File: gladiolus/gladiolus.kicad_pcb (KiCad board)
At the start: 4 copper layers, 70.7 x 53.3 mm, 138 parts, among them J1 NEIGHBOR1, J2 NEIGHBOR2, J3 Conn_01x02_Female, J7 BONUS_ROW, Q1 Q_NPN_BEC, U1 THS4520RGT, U2 AD8330ARQZ, U3 AD9283, U4 AD9704, U5 LMH6643, U6 74LVC1G3157, U7 74LVC1G3157

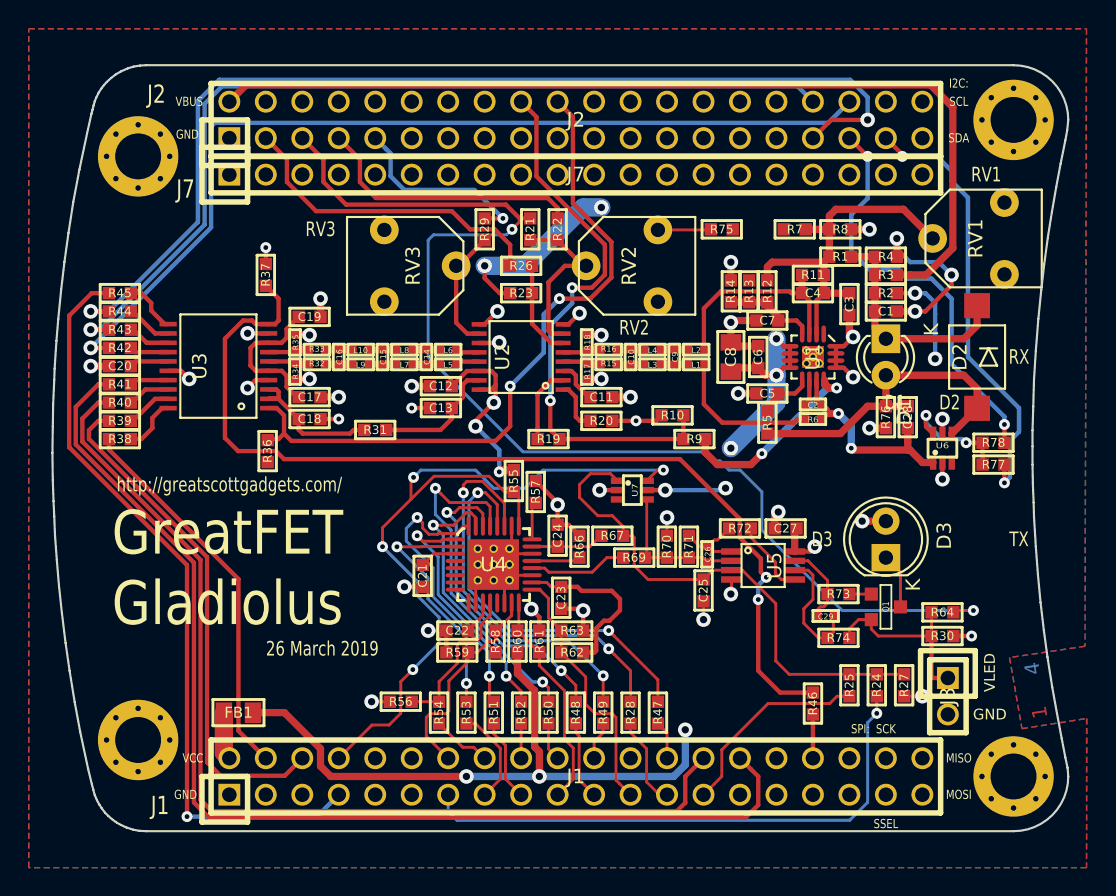
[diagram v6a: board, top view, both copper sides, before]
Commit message: Rerouted ADC trace to improve ground plane connectivity
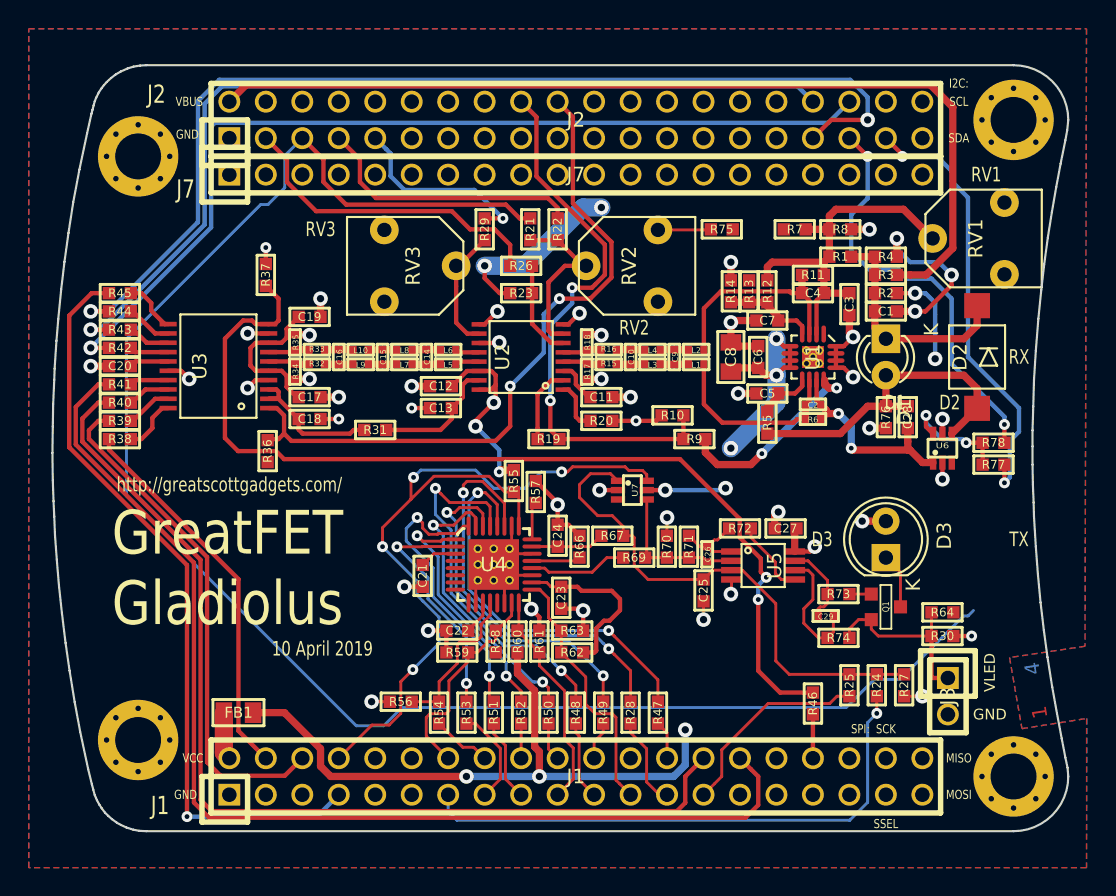
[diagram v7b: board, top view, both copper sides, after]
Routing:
- net /ADC0_0: track 83.9 -> 118.3 mm, vias 2 -> 0
- net /P5_0: track 56.6 -> 54.7 mm
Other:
- board text added: "10 April 2019"
- board text removed: "26 March 2019"
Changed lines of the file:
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@@
     (thickness 1.6)
     (drawings 133)
-    (tracks 1068)
+    (tracks 1066)
     (zones 0)
     (modules 138)
@@
     (pad_drill 0.762)
     (pad_to_mask_clearance 0.127)
-    (solder_mask_min_width 0.25)
     (pad_to_paste_clearance_ratio -0.05)
     (aux_axis_origin 0 0)
@@
   (gr_line (start 177.9016 92.3544) (end 177.8508 94.0054) (angle 90) (layer Edge.Cuts) (width 0.15))
   (gr_line (start 177.9524 90.5002) (end 177.9016 92.3544) (angle 90) (layer Edge.Cuts) (width 0.15))
-  (gr_text "26 March 2019" (at 128.397 109.22) (layer F.SilkS)
+  (gr_text "10 April 2019" (at 128.397 109.22) (layer F.SilkS)
     (effects (font (size 1.016 0.762) (thickness 0.1524)))
   )
@@
   (segment (start 134.569198 98.806) (end 132.588 100.787198) (width 0.2032) (layer F.Cu) (net 26))
   (segment (start 136.169411 97.205787) (end 134.569198 98.806) (width 0.2032) (layer F.Cu) (net 26))
-  (via (at 152.146 96.774) (size 0.762) (drill 0.3302) (layers F.Cu B.Cu) (net 26))
-  (segment (start 151.734 96.774) (end 150.987 97.521) (width 0.2032) (layer F.Cu) (net 26) (status 20))
-  (segment (start 152.146 96.774) (end 151.734 96.774) (width 0.2032) (layer F.Cu) (net 26))
+  (segment (start 150.987 97.0928) (end 150.6936 96.7994) (width 0.2032) (layer F.Cu) (net 26))
+  (segment (start 150.987 97.521) (end 150.987 97.0928) (width 0.2032) (layer F.Cu) (net 26))
+  (segment (start 149.733 96.7994) (end 149.479 96.5454) (width 0.2032) (layer F.Cu) (net 26))
+  (segment (start 150.6936 96.7994) (end 149.733 96.7994) (width 0.2032) (layer F.Cu) (net 26))
+  (segment (start 149.479 96.5454) (end 145.8214 96.5454) (width 0.2032) (layer F.Cu) (net 26))
+  (via (at 145.0594 96.901) (size 0.762) (drill 0.3302) (layers F.Cu B.Cu) (net 26))
+  (segment (start 145.8214 96.5454) (end 145.4658 96.901) (width 0.2032) (layer F.Cu) (net 26))
+  (segment (start 145.4658 96.901) (end 145.0594 96.901) (width 0.2032) (layer F.Cu) (net 26))
   (segment (start 140.335 98.044) (end 139.065 96.774) (width 0.2032) (layer B.Cu) (net 26))
   (segment (start 135.255 96.774) (end 134.747 97.282) (width 0.2032) (layer B.Cu) (net 26))
-  (segment (start 139.065 96.774) (end 135.255 96.774) (width 0.2032) (layer B.Cu) (net 26))
   (segment (start 142.494 98.044) (end 140.335 98.044) (width 0.2032) (layer B.Cu) (net 26))
-  (segment (start 143.764 96.774) (end 142.494 98.044) (width 0.2032) (layer B.Cu) (net 26))
-  (segment (start 152.146 96.774) (end 143.764 96.774) (width 0.2032) (layer B.Cu) (net 26))
+  (segment (start 143.637 96.901) (end 142.494 98.044) (width 0.2032) (layer B.Cu) (net 26))
+  (segment (start 139.065 96.774) (end 135.255 96.774) (width 0.2032) (layer B.Cu) (net 26))
+  (segment (start 145.0594 96.901) (end 143.637 96.901) (width 0.2032) (layer B.Cu) (net 26))
   (segment (start 137.16 119.38) (end 137.16 120.5484) (width 0.2032) (layer B.Cu) (net 27) (status 10))
   (segment (start 137.16 120.5484) (end 137.7696 121.158) (width 0.2032) (layer B.Cu) (net 27))
@@
   (segment (start 128.473199 75.133199) (end 128.473199 76.712065) (width 0.3048) (layer F.Cu) (net 45))
   (segment (start 128.473199 76.712065) (end 130.049123 78.287989) (width 0.3048) (layer F.Cu) (net 45))
-  (segment (start 142.24 79.248) (end 142.113 79.375) (width 0.2032) (layer F.Cu) (net 45))
-  (segment (start 142.875 79.248) (end 142.24 79.248) (width 0.2032) (layer F.Cu) (net 45) (status 10))
-  (via (at 141.605 80.01) (size 0.762) (drill 0.3302) (layers F.Cu B.Cu) (net 45))
-  (segment (start 142.113 79.375) (end 142.113 79.502) (width 0.2032) (layer F.Cu) (net 45))
-  (segment (start 142.113 79.502) (end 141.605 80.01) (width 0.2032) (layer F.Cu) (net 45))
-  (via (at 173.736 106.553) (size 0.762) (drill 0.3302) (layers F.Cu B.Cu) (net 45))
-  (segment (start 172.466 106.553) (end 172.339 106.68) (width 0.2032) (layer F.Cu) (net 45) (status 30))
-  (segment (start 173.99 106.553) (end 172.466 106.553) (width 0.2032) (layer F.Cu) (net 45) (status 20))
-  (segment (start 164.592 106.553) (end 173.99 106.553) (width 0.2032) (layer B.Cu) (net 45))
-  (segment (start 159.004 100.965) (end 164.592 106.553) (width 0.2032) (layer B.Cu) (net 45))
-  (segment (start 159.004 98.298) (end 159.004 100.965) (width 0.2032) (layer B.Cu) (net 45))
-  (segment (start 156.718 96.774) (end 157.48 96.774) (width 0.2032) (layer B.Cu) (net 45))
-  (segment (start 156.083 96.139) (end 156.718 96.774) (width 0.2032) (layer B.Cu) (net 45))
-  (segment (start 154.813 95.504) (end 155.448 96.139) (width 0.2032) (layer B.Cu) (net 45))
-  (segment (start 157.48 96.774) (end 159.004 98.298) (width 0.2032) (layer B.Cu) (net 45))
-  (segment (start 141.605 80.01) (end 141.224 80.391) (width 0.2032) (layer B.Cu) (net 45))
-  (segment (start 155.448 96.139) (end 156.083 96.139) (width 0.2032) (layer B.Cu) (net 45))
-  (segment (start 136.144 80.391) (end 135.763 80.772) (width 0.2032) (layer B.Cu) (net 45))
-  (segment (start 135.763 80.772) (end 135.763 88.9) (width 0.2032) (layer B.Cu) (net 45))
-  (segment (start 135.763 88.9) (end 142.367 95.504) (width 0.2032) (layer B.Cu) (net 45))
-  (segment (start 141.224 80.391) (end 136.144 80.391) (width 0.2032) (layer B.Cu) (net 45))
-  (segment (start 142.367 95.504) (end 154.813 95.504) (width 0.2032) (layer B.Cu) (net 45))
+  (segment (start 173.355001 106.933999) (end 173.050201 106.933999) (width 0.2032) (layer B.Cu) (net 45))
+  (segment (start 173.736 106.553) (end 173.355001 106.933999) (width 0.2032) (layer B.Cu) (net 45))
+  (segment (start 173.050201 106.933999) (end 168.6306 111.3536) (width 0.2032) (layer B.Cu) (net 45))
+  (segment (start 168.6306 111.3536) (end 166.8272 111.3536) (width 0.2032) (layer B.Cu) (net 45))
+  (segment (start 166.8272 111.3536) (end 164.8714 113.3094) (width 0.2032) (layer B.Cu) (net 45))
+  (segment (start 164.8714 113.3094) (end 133.9342 113.3094) (width 0.2032) (layer B.Cu) (net 45))
+  (segment (start 133.9342 113.3094) (end 132.6642 114.5794) (width 0.2032) (layer B.Cu) (net 45))
+  (segment (start 132.6642 114.5794) (end 130.7592 114.5794) (width 0.2032) (layer B.Cu) (net 45))
+  (segment (start 130.7592 114.5794) (end 114.7572 98.5774) (width 0.2032) (layer B.Cu) (net 45))
+  (segment (start 114.7572 98.5774) (end 114.7572 87.63) (width 0.2032) (layer B.Cu) (net 45))
+  (segment (start 114.7572 87.63) (end 124.1044 78.2828) (width 0.2032) (layer B.Cu) (net 45))
+  (segment (start 124.1044 78.2828) (end 124.6124 78.2828) (width 0.2032) (layer B.Cu) (net 45))
+  (segment (start 124.6124 78.2828) (end 125.7808 77.1144) (width 0.2032) (layer B.Cu) (net 45))
+  (segment (start 125.7808 74.8792) (end 127 73.66) (width 0.2032) (layer B.Cu) (net 45))
+  (segment (start 125.7808 77.1144) (end 125.7808 74.8792) (width 0.2032) (layer B.Cu) (net 45))
   (segment (start 132.131913 77.830779) (end 144.099379 77.830779) (width 0.3048) (layer F.Cu) (net 46))
   (segment (start 144.099379 77.830779) (end 144.78 78.5114) (width 0.3048) (layer F.Cu) (net 46))

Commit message: Changed switch to turn off TX while the DAC is in sleep mode.
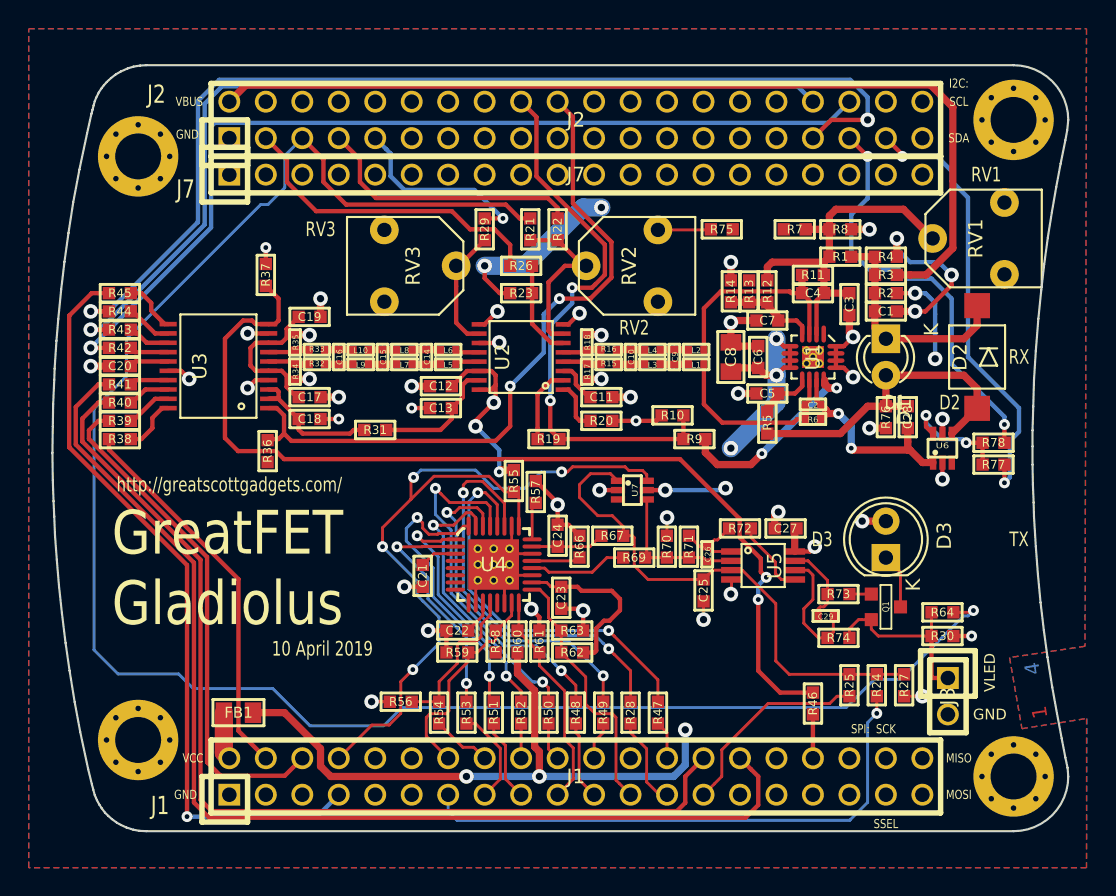
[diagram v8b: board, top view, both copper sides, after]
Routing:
- net /ADC0_0: track 118.3 -> 129.3 mm, vias 0 -> 1
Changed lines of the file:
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@@
     (thickness 1.6)
     (drawings 133)
-    (tracks 1066)
+    (tracks 1075)
     (zones 0)
     (modules 138)
@@
     (pad_drill 0.762)
     (pad_to_mask_clearance 0.127)
+    (solder_mask_min_width 0.25)
     (pad_to_paste_clearance_ratio -0.05)
     (aux_axis_origin 0 0)
@@
   (segment (start 128.473199 75.133199) (end 128.473199 76.712065) (width 0.3048) (layer F.Cu) (net 45))
   (segment (start 128.473199 76.712065) (end 130.049123 78.287989) (width 0.3048) (layer F.Cu) (net 45))
-  (segment (start 173.355001 106.933999) (end 173.050201 106.933999) (width 0.2032) (layer B.Cu) (net 45))
-  (segment (start 173.736 106.553) (end 173.355001 106.933999) (width 0.2032) (layer B.Cu) (net 45))
-  (segment (start 173.050201 106.933999) (end 168.6306 111.3536) (width 0.2032) (layer B.Cu) (net 45))
+  (via (at 173.736 106.553) (size 0.762) (drill 0.3302) (layers F.Cu B.Cu) (net 45))
+  (segment (start 172.339 106.68) (end 173.609 106.68) (width 0.2032) (layer F.Cu) (net 45))
+  (segment (start 173.609 106.68) (end 173.736 106.553) (width 0.2032) (layer F.Cu) (net 45))
+  (segment (start 125.7808 74.8792) (end 127 73.66) (width 0.2032) (layer B.Cu) (net 45))
+  (segment (start 125.7808 77.1144) (end 125.7808 74.8792) (width 0.2032) (layer B.Cu) (net 45))
+  (segment (start 124.6124 78.2828) (end 125.7808 77.1144) (width 0.2032) (layer B.Cu) (net 45))
+  (segment (start 127.5334 114.5794) (end 124.9426 111.9886) (width 0.2032) (layer B.Cu) (net 45))
   (segment (start 168.6306 111.3536) (end 166.8272 111.3536) (width 0.2032) (layer B.Cu) (net 45))
-  (segment (start 166.8272 111.3536) (end 164.8714 113.3094) (width 0.2032) (layer B.Cu) (net 45))
   (segment (start 164.8714 113.3094) (end 133.9342 113.3094) (width 0.2032) (layer B.Cu) (net 45))
+  (segment (start 166.8272 111.3536) (end 164.8714 113.3094) (width 0.2032) (layer B.Cu) (net 45))
+  (segment (start 119.4054 111.9886) (end 118.3894 110.9726) (width 0.2032) (layer B.Cu) (net 45))
+  (segment (start 124.1044 78.2828) (end 124.6124 78.2828) (width 0.2032) (layer B.Cu) (net 45))
+  (segment (start 112.4966 109.2962) (end 112.4966 92.5068) (width 0.2032) (layer B.Cu) (net 45))
+  (segment (start 173.736 106.553) (end 173.355001 106.933999) (width 0.2032) (layer B.Cu) (net 45))
   (segment (start 133.9342 113.3094) (end 132.6642 114.5794) (width 0.2032) (layer B.Cu) (net 45))
-  (segment (start 132.6642 114.5794) (end 130.7592 114.5794) (width 0.2032) (layer B.Cu) (net 45))
-  (segment (start 130.7592 114.5794) (end 114.7572 98.5774) (width 0.2032) (layer B.Cu) (net 45))
-  (segment (start 114.7572 98.5774) (end 114.7572 87.63) (width 0.2032) (layer B.Cu) (net 45))
+  (segment (start 114.173 110.9726) (end 112.4966 109.2962) (width 0.2032) (layer B.Cu) (net 45))
+  (segment (start 173.050201 106.933999) (end 168.6306 111.3536) (width 0.2032) (layer B.Cu) (net 45))
+  (segment (start 173.355001 106.933999) (end 173.050201 106.933999) (width 0.2032) (layer B.Cu) (net 45))
+  (segment (start 114.7572 90.2462) (end 114.7572 87.63) (width 0.2032) (layer B.Cu) (net 45))
+  (segment (start 132.6642 114.5794) (end 127.5334 114.5794) (width 0.2032) (layer B.Cu) (net 45))
+  (segment (start 124.9426 111.9886) (end 119.4054 111.9886) (width 0.2032) (layer B.Cu) (net 45))
   (segment (start 114.7572 87.63) (end 124.1044 78.2828) (width 0.2032) (layer B.Cu) (net 45))
-  (segment (start 124.1044 78.2828) (end 124.6124 78.2828) (width 0.2032) (layer B.Cu) (net 45))
-  (segment (start 124.6124 78.2828) (end 125.7808 77.1144) (width 0.2032) (layer B.Cu) (net 45))
-  (segment (start 125.7808 74.8792) (end 127 73.66) (width 0.2032) (layer B.Cu) (net 45))
-  (segment (start 125.7808 77.1144) (end 125.7808 74.8792) (width 0.2032) (layer B.Cu) (net 45))
+  (segment (start 118.3894 110.9726) (end 114.173 110.9726) (width 0.2032) (layer B.Cu) (net 45))
+  (segment (start 112.4966 92.5068) (end 114.7572 90.2462) (width 0.2032) (layer B.Cu) (net 45))
   (segment (start 132.131913 77.830779) (end 144.099379 77.830779) (width 0.3048) (layer F.Cu) (net 46))
   (segment (start 144.099379 77.830779) (end 144.78 78.5114) (width 0.3048) (layer F.Cu) (net 46))
